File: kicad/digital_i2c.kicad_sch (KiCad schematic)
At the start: 28 parts, among them J10 Qwiic Cell Density, J11 Qwiic EZO-pH, J12 Qwiic EZO-ORP, J13 Qwiic EZO-DO, J14 Qwiic EZO-RTD, J15 Load Cell, J16 RS485 Hamilton, J8 Qwiic GPS SAM-M8Q, J9 Qwiic RTC DS3231, U14 HX711, U15 MAX3485CSA, U21 ISO1541, U22 SC16IS740, U23 SN74LVC1G04, Y1 1.8432MHz

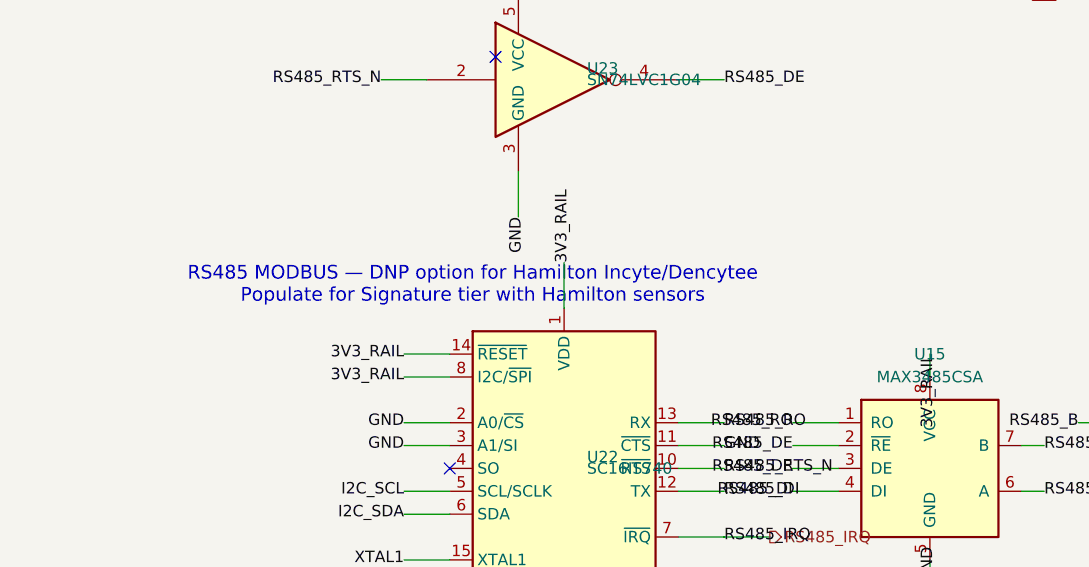
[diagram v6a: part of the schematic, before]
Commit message: feat(sch,pcb,docs): redefine tiers Essential/Insight/Signature and sync DNP
- Tier mapping:
  - Essential: GPS, RTC/timestamp, temperature, pH, ORP
  - Insight: Essential + CO2 pressure (A4), DO (A5), HX711 load cell,
    chiller, recirculation motor, gas solenoid (single gas via K1/J18)
  - Signature: Insight + Hamilton TCD + ACD via RS485 bridge
- Humidity channel (J7/D8/R17/R18/C23) and PWM gas valve (U20/Q5/D14/R28/C27/J22)
  marked DNP in all tiers.
- Update DNP properties in kicad/analog_acquisition.kicad_sch,
  kicad/digital_i2c.kicad_sch, kicad/actuator_drivers.kicad_sch,
  kicad/power_management.kicad_sch using kicad/tier_dnp_mapping.json.
- Update sheet comments and root text block.
- Update docs/04_BOM_PRODUCTION.md section 11, docs/INSIGHT_FABRICATION_ROADMAP.md,
  and docs/DOCUMENTATION_UPDATE_AUDIT.md.
- Add helper tools: build_tier_map.py, apply_tier_dnp4.py, update_tier_comments.py,
  list_actual_components.py, tier_counts.py, validate_sch.py, count_parens.py.
- Sync current PCB state (component positions/nets) to match corrected netlist.

Validation:
- kicad-cli sch erc --severity-all: 0 violaciones
- kicad-cli pcb drc --severity-error: 0 violaciones, 332 unconnected items
- compare_pcb_to_netlist.py: 0 parity problems

Co-Authored-By: Devin AI <158243242+devin-ai-integration[bot]@users.noreply.github.com>
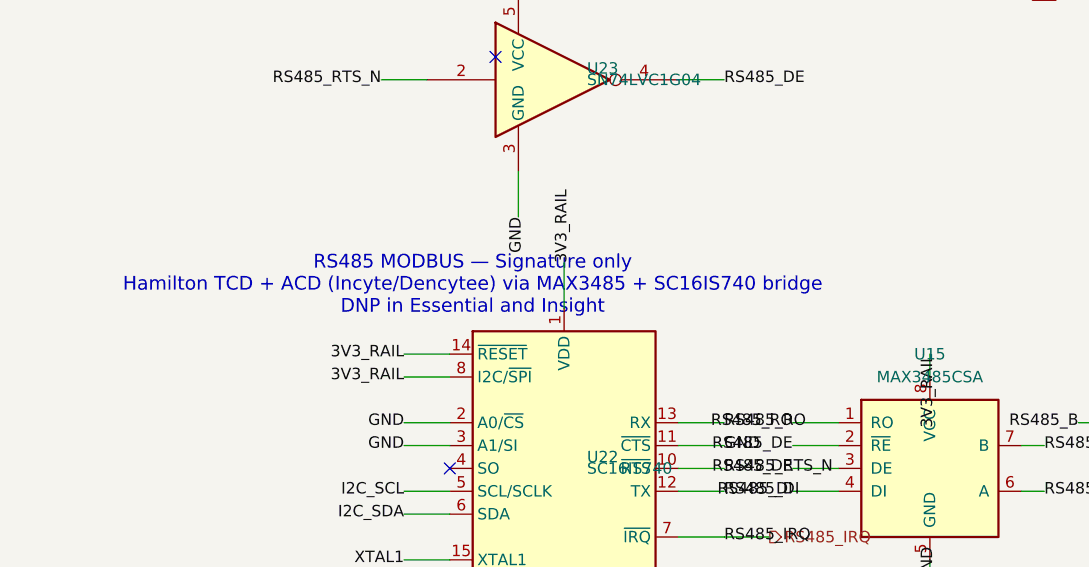
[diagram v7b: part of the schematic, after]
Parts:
- C25, C26, J15, R21, U14: DNP (none) -> Essential
- C31, C32, C33, R38, U22, U23, Y1: DNP (none) -> Essential,Insight
- D9, LED4, R19, R20, R23, U21: DNP (none) -> NO
- J10: DNP Signature -> Essential,Insight,Signature
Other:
- note added: "RS485 MODBUS — Signature only Hamilton TCD + ACD (Incyte/Dencytee) via MAX3485 + SC16IS740 bridge DNP in Essential and Insight"
- note removed: "RS485 MODBUS — DNP option for Hamilton Incyte/Dencytee Populate for Signature tier with Hamilton sensors"
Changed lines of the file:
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@@
     (rev "1.0")
     (company "Cafelium SRL / Nebula Ecosystem")
-    (comment 1 "Sheet 3 of 5: I2C Bus, HX711 Load Cell, RS485 (DNP), Status LED")
-    (comment 2 "I2C devices: GPS(0x42), RTC(0x68), Cell Density(0x30), EZO optional")
+    (comment 1 "Sheet 3 of 5: I2C Bus, HX711 Load Cell (Insight+), RS485 (Signature), Status LED")
+    (comment 2 "I2C: GPS(0x42), RTC(0x68), EZO optional; HX711 J15 DNP Essential; RS485 J16 Signature; J10 DNP all tiers")
   )
   (text "I2C BUS — 400 kHz Fast Mode\nPull-ups 4.7k to 3.3V, ESD protection PESD3V3S2USF"
@@
     (exclude_from_sim no) (in_bom yes) (on_board yes)
     (property "Reference" "R19" (at 53.34 43.18 0) (effects (font (size 1.27 1.27)) (justify left)))
+    (property "DNP" "NO" (at 0 0 0) (effects (font (size 1.27 1.27)) hide))
     (property "Value" "4.7k 1%" (at 53.34 44.45 0) (effects (font (size 1.27 1.27)) (justify left)))
     (property "Footprint" "Resistor_SMD:R_0402_1005Metric" (at 50.8 43.18 0) (effects (font (size 1.27 1.27)) hide))
@@
     (exclude_from_sim no) (in_bom yes) (on_board yes)
     (property "Reference" "R20" (at 66.04 43.18 0) (effects (font (size 1.27 1.27)) (justify left)))
+    (property "DNP" "NO" (at 0 0 0) (effects (font (size 1.27 1.27)) hide))
     (property "Value" "4.7k 1%" (at 66.04 44.45 0) (effects (font (size 1.27 1.27)) (justify left)))
     (property "Footprint" "Resistor_SMD:R_0402_1005Metric" (at 63.5 43.18 0) (effects (font (size 1.27 1.27)) hide))
@@
     (exclude_from_sim no) (in_bom yes) (on_board yes)
     (property "Reference" "D9" (at 50.8 53.34 0) (effects (font (size 1.27 1.27))))
+    (property "DNP" "NO" (at 0 0 0) (effects (font (size 1.27 1.27)) hide))
     (property "Value" "PESD3V3S2USF" (at 50.8 55.88 0) (effects (font (size 1.27 1.27))))
     (property "Footprint" "Package_TO_SOT_SMD:SOT-23-3" (at 50.8 58.42 0) (effects (font (size 1.27 1.27)) hide))
@@
     (property "Description" "JST-SH Qwiic: VCC/GND/SDA/SCL — Cell Density I2C addr 0x30"
       (at 88.9 111.76 0) (effects (font (size 1.27 1.27)) hide))
-    (property "DNP" "Signature"
+    (property "DNP" "Essential,Insight,Signature"
       (at 88.9 111.76 0) (effects (font (size 1.27 1.27)) hide))
     (pin "1")
@@
     (exclude_from_sim no) (in_bom yes) (on_board yes)
     (property "Reference" "U14" (at 195.58 40.64 0) (effects (font (size 1.27 1.27))))
+    (property "DNP" "Essential" (at 0 0 0) (effects (font (size 1.27 1.27)) hide))
     (property "Value" "HX711" (at 195.58 43.18 0) (effects (font (size 1.27 1.27))))
     (property "Footprint" "Package_SO:SOP-16_4.4x10.4mm_P1.27mm" (at 195.58 55.88 0) (effects (font (size 1.27 1.27)) hide))
@@
     (exclude_from_sim no) (in_bom yes) (on_board yes)
     (property "Reference" "J15" (at 233.68 46.99 0) (effects (font (size 1.27 1.27))))
+    (property "DNP" "Essential" (at 0 0 0) (effects (font (size 1.27 1.27)) hide))
     (property "Value" "Load Cell" (at 233.68 48.26 0) (effects (font (size 1.27 1.27))))
     (property "Footprint" "TerminalBlock_Phoenix:TerminalBlock_Phoenix_PT-1,5-4-5.0-H_1x04_P5.00mm_Horizontal"
@@
     (exclude_from_sim no) (in_bom yes) (on_board yes)
     (property "Reference" "R21" (at 215.9 43.18 0) (effects (font (size 1.27 1.27)) (justify left)))
+    (property "DNP" "Essential" (at 0 0 0) (effects (font (size 1.27 1.27)) hide))
     (property "Value" "10k" (at 215.9 44.45 0) (effects (font (size 1.27 1.27)) (justify left)))
     (property "Footprint" "Resistor_SMD:R_0402_1005Metric" (at 213.36 43.18 0) (effects (font (size 1.27 1.27)) hide))
@@
     (exclude_from_sim no) (in_bom yes) (on_board yes)
     (property "Reference" "C25" (at 185.42 68.58 0) (effects (font (size 1.27 1.27)) (justify left)))
+    (property "DNP" "Essential" (at 0 0 0) (effects (font (size 1.27 1.27)) hide))
     (property "Value" "100nF" (at 185.42 69.85 0) (effects (font (size 1.27 1.27)) (justify left)))
     (property "Footprint" "Capacitor_SMD:C_0402_1005Metric" (at 182.88 68.58 0) (effects (font (size 1.27 1.27)) hide))
@@
     (exclude_from_sim no) (in_bom yes) (on_board yes)
     (property "Reference" "C26" (at 175.26 68.58 0) (effects (font (size 1.27 1.27)) (justify right)))
+    (property "DNP" "Essential" (at 0 0 0) (effects (font (size 1.27 1.27)) hide))
     (property "Value" "10uF" (at 175.26 69.85 0) (effects (font (size 1.27 1.27)) (justify right)))
     (property "Footprint" "Capacitor_SMD:C_0805_2012Metric" (at 177.8 68.58 0) (effects (font (size 1.27 1.27)) hide))
@@
     )
   )
-  (text "RS485 MODBUS — DNP option for Hamilton Incyte/Dencytee\nPopulate for Signature tier with Hamilton sensors"
+  (text "RS485 MODBUS — Signature only\nHamilton TCD + ACD (Incyte/Dencytee) via MAX3485 + SC16IS740 bridge\nDNP in Essential and Insight"
     (at 25.4 220.98 0)
     (effects (font (size 1.524 1.524)))
@@
     (exclude_from_sim no) (in_bom yes) (on_board yes)
     (property "Reference" "LED4" (at 170.18 213.36 0) (effects (font (size 1.27 1.27))))
+    (property "DNP" "NO" (at 0 0 0) (effects (font (size 1.27 1.27)) hide))
     (property "Value" "Red/Green" (at 170.18 215.9 0) (effects (font (size 1.27 1.27))))
     (property "Footprint" "LED_SMD:LED_0603_1608Metric" (at 170.18 220.98 0) (effects (font (size 1.27 1.27)) hide))
@@
     (exclude_from_sim no) (in_bom yes) (on_board yes)
     (property "Reference" "R23" (at 172.72 208.28 0) (effects (font (size 1.27 1.27)) (justify left)))
+    (property "DNP" "NO" (at 0 0 0) (effects (font (size 1.27 1.27)) hide))
     (property "Value" "330R" (at 172.72 209.55 0) (effects (font (size 1.27 1.27)) (justify left)))
     (property "Footprint" "Resistor_SMD:R_0402_1005Metric" (at 170.18 208.28 0) (effects (font (size 1.27 1.27)) hide))
@@
   (symbol (lib_id "Isolator:ISO1541") (at 149.86 121.92 0) (unit 1) (exclude_from_sim no) (in_bom yes) (on_board yes)
     (property "Reference" "U21" (at 149.86 109.22 0) (effects (font (size 1.27 1.27))))
+    (property "DNP" "NO" (at 0 0 0) (effects (font (size 1.27 1.27)) hide))
     (property "Value" "ISO1541" (at 149.86 111.76 0) (effects (font (size 1.27 1.27))))
     (property "Footprint" "Package_SO:SOIC-8_3.9x4.9mm_P1.27mm" (at 149.86 121.92 0) (effects (font (size 1.27 1.27)) hide))
@@
       (exclude_from_sim no) (in_bom yes) (on_board yes)
       (property "Reference" "U22" (at 38.10 240.03 0) (effects (font (size 1.27 1.27)) (justify left)))
+      (property "DNP" "Essential,Insight" (at 0 0 0) (effects (font (size 1.27 1.27)) hide))
       (property "Value" "SC16IS740" (at 38.10 241.30 0) (effects (font (size 1.27 1.27)) (justify left)))
       (property "Footprint" "Package_SO:TSSOP-16_4.4x5mm_P0.65mm" (at 35.56 241.30 0) (effects (font (size 1.27 1.27)) hide))
@@
       (exclude_from_sim no) (in_bom yes) (on_board yes)
       (property "Reference" "U23" (at 38.10 196.85 0) (effects (font (size 1.27 1.27)) (justify left)))
+      (property "DNP" "Essential,Insight" (at 0 0 0) (effects (font (size 1.27 1.27)) hide))
       (property "Value" "SN74LVC1G04" (at 38.10 198.12 0) (effects (font (size 1.27 1.27)) (justify left)))
       (property "Footprint" "Package_TO_SOT_SMD:SOT-353_SC-70-5" (at 35.56 198.12 0) (effects (font (size 1.27 1.27)) hide))
@@
       (exclude_from_sim no) (in_bom yes) (on_board yes)
       (property "Reference" "Y1" (at 139.70 227.33 0) (effects (font (size 1.27 1.27)) (justify left)))
+      (property "DNP" "Essential,Insight" (at 0 0 0) (effects (font (size 1.27 1.27)) hide))
       (property "Value" "1.8432MHz" (at 139.70 228.60 0) (effects (font (size 1.27 1.27)) (justify left)))
       (property "Footprint" "Crystal:Crystal_SMD_HC49-SD" (at 137.16 228.60 0) (effects (font (size 1.27 1.27)) hide))
@@
       (exclude_from_sim no) (in_bom yes) (on_board yes)
       (property "Reference" "C31" (at 139.70 240.03 0) (effects (font (size 1.27 1.27)) (justify left)))
+      (property "DNP" "Essential,Insight" (at 0 0 0) (effects (font (size 1.27 1.27)) hide))
       (property "Value" "22pF C0G" (at 139.70 241.30 0) (effects (font (size 1.27 1.27)) (justify left)))
       (property "Footprint" "Capacitor_SMD:C_0402_1005Metric" (at 137.16 241.30 0) (effects (font (size 1.27 1.27)) hide))
@@
       (exclude_from_sim no) (in_bom yes) (on_board yes)
       (property "Reference" "C32" (at 152.40 240.03 0) (effects (font (size 1.27 1.27)) (justify left)))
+      (property "DNP" "Essential,Insight" (at 0 0 0) (effects (font (size 1.27 1.27)) hide))
       (property "Value" "22pF C0G" (at 152.40 241.30 0) (effects (font (size 1.27 1.27)) (justify left)))
       (property "Footprint" "Capacitor_SMD:C_0402_1005Metric" (at 149.86 241.30 0) (effects (font (size 1.27 1.27)) hide))
@@
       (exclude_from_sim no) (in_bom yes) (on_board yes)
       (property "Reference" "C33" (at 165.10 240.03 0) (effects (font (size 1.27 1.27)) (justify left)))
+      (property "DNP" "Essential,Insight" (at 0 0 0) (effects (font (size 1.27 1.27)) hide))
       (property "Value" "100nF X7R" (at 165.10 241.30 0) (effects (font (size 1.27 1.27)) (justify left)))
       (property "Footprint" "Capacitor_SMD:C_0402_1005Metric" (at 162.56 241.30 0) (effects (font (size 1.27 1.27)) hide))
@@
       (exclude_from_sim no) (in_bom yes) (on_board yes)
       (property "Reference" "R38" (at 177.80 240.03 0) (effects (font (size 1.27 1.27)) (justify left)))
+      (property "DNP" "Essential,Insight" (at 0 0 0) (effects (font (size 1.27 1.27)) hide))
       (property "Value" "10k 1%" (at 177.80 241.30 0) (effects (font (size 1.27 1.27)) (justify left)))
       (property "Footprint" "Resistor_SMD:R_0402_1005Metric" (at 175.26 241.30 0) (effects (font (size 1.27 1.27)) hide))
